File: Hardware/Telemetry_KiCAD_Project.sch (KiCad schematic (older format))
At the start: 3 parts, among them J1 TX SPI Debug, J2 RX SPI Debug, J3 50Ω SMA Connector

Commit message: Placed RF traces w/rounded corners
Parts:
- J1, J2: footprint Connector_PinHeader_2.54mm:PinHeader_2x03_P2.54mm_Vertical -> Connector_PinHeader_2.54mm:PinHeader_2x04_P2.54mm_Vertical; symbol Connector_Generic:Conn_02x03_Odd_Even -> Connector_Generic:Conn_02x04_Odd_Even
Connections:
- net GND: now also J1.8 (Pin_8), J2.8 (Pin_8); no longer J1.6 (Pin_6), J2.6 (Pin_6)
- net RX_RST: now also J2.1 (Pin_1)
- net RX_SCL: now also J2.5 (Pin_5); no longer J2.4 (Pin_4)
- net RX_SDI: now also J2.3 (Pin_3); no longer J2.2 (Pin_2)
- net RX_SDO: now also J2.4 (Pin_4); no longer J2.5 (Pin_5)
- net TX_RST: now also J1.1 (Pin_1)
- net TX_SCL: now also J1.5 (Pin_5); no longer J1.4 (Pin_4)
- net TX_SDI: now also J1.3 (Pin_3); no longer J1.2 (Pin_2)
- net TX_SDO: now also J1.4 (Pin_4); no longer J1.5 (Pin_5)
- net ~RX_IRQ: now also J2.6 (Pin_6); no longer J2.3 (Pin_3)
- net ~RX_SEL: now also J2.2 (Pin_2); no longer J2.1 (Pin_1)
- net ~TX_IRQ: now also J1.6 (Pin_6); no longer J1.3 (Pin_3)
- net ~TX_SEL: now also J1.2 (Pin_2); no longer J1.1 (Pin_1)
- no-connect marks 1 -> 3
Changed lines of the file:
@@
 	7050 3900 8350 3900
 $Comp
-L Connector_Generic:Conn_02x03_Odd_Even J1
-U 1 1 61BF0412
-P 4250 950
-F 0 "J1" H 4300 1267 50  0000 C CNN
-F 1 "TX SPI Debug" H 4300 1176 50  0000 C CNN
-F 2 "Connector_PinHeader_2.54mm:PinHeader_2x03_P2.54mm_Vertical" H 4250 950 50  0001 C CNN
-F 3 "~" H 4250 950 50  0001 C CNN
-	1    4250 950
-	1    0    0    -1
-$EndComp
-$Comp
-L Connector_Generic:Conn_02x03_Odd_Even J2
+L Connector_Generic:Conn_02x04_Odd_Even J2
 U 1 1 61BF15AF
 P 5750 950
 F 0 "J2" H 5800 1267 50  0000 C CNN
 F 1 "RX SPI Debug" H 5800 1176 50  0000 C CNN
-F 2 "Connector_PinHeader_2.54mm:PinHeader_2x03_P2.54mm_Vertical" H 5750 950 50  0001 C CNN
+F 2 "Connector_PinHeader_2.54mm:PinHeader_2x04_P2.54mm_Vertical" H 5750 950 50  0001 C CNN
 F 3 "~" H 5750 950 50  0001 C CNN
 	1    5750 950
 	1    0    0    -1
 $EndComp
-Text Label 4050 850  2    50   ~ 0
+Text Label 4550 850  0    50   ~ 0
 ~TX_SEL
+Text Label 4550 1050 0    50   ~ 0
+~TX_IRQ
+Text Label 4550 950  0    50   ~ 0
+TX_SDO
 Text Label 4050 950  2    50   ~ 0
-~TX_IRQ
+TX_SDI
 Text Label 4050 1050 2    50   ~ 0
-TX_SDO
-Text Label 4550 850  0    50   ~ 0
-TX_SDI
-Text Label 4550 950  0    50   ~ 0
 TX_SCL
-$Comp
-L power:GND #PWR01
-U 1 1 61BF6E76
-P 4550 1050
-F 0 "#PWR01" H 4550 800 50  0001 C CNN
-F 1 "GND" H 4555 877 50  0000 C CNN
-F 2 "" H 4550 1050 50  0001 C CNN
-F 3 "" H 4550 1050 50  0001 C CNN
-	1    4550 1050
-	1    0    0    -1
-$EndComp
-Text Label 5550 850  2    50   ~ 0
+Text Label 6050 850  0    50   ~ 0
 ~RX_SEL
+Text Label 6050 1050 0    50   ~ 0
+~RX_IRQ
+Text Label 6050 950  0    50   ~ 0
+RX_SDO
 Text Label 5550 950  2    50   ~ 0
-~RX_IRQ
+RX_SDI
 Text Label 5550 1050 2    50   ~ 0
-RX_SDO
-Text Label 6050 850  0    50   ~ 0
-RX_SDI
-Text Label 6050 950  0    50   ~ 0
 RX_SCL
 $Comp
 L power:GND #PWR02
 U 1 1 61BF7DA6
-P 6050 1050
-F 0 "#PWR02" H 6050 800 50  0001 C CNN
-F 1 "GND" H 6055 877 50  0000 C CNN
-F 2 "" H 6050 1050 50  0001 C CNN
-F 3 "" H 6050 1050 50  0001 C CNN
-	1    6050 1050
+P 6050 1150
+F 0 "#PWR02" H 6050 900 50  0001 C CNN
+F 1 "GND" H 6055 977 50  0000 C CNN
+F 2 "" H 6050 1150 50  0001 C CNN
+F 3 "" H 6050 1150 50  0001 C CNN
+	1    6050 1150
 	1    0    0    -1
 $EndComp
@@
 Entry Wire Line
 	6350 850  6450 950
-Entry Wire Line
-	6350 950  6450 1050
 Wire Bus Line
 	4800 2250 5550 2250
@@
 Text Label 6250 4400 2    50   ~ 0
 RX_RST
+$Comp
+L Connector_Generic:Conn_02x04_Odd_Even J1
+U 1 1 61BF0412
+P 4250 950
+F 0 "J1" H 4300 1267 50  0000 C CNN
+F 1 "TX SPI Debug" H 4300 1176 50  0000 C CNN
+F 2 "Connector_PinHeader_2.54mm:PinHeader_2x04_P2.54mm_Vertical" H 4250 950 50  0001 C CNN
+F 3 "~" H 4250 950 50  0001 C CNN
+	1    4250 950
+	1    0    0    -1
+$EndComp
+$Comp
+L power:GND #PWR01
+U 1 1 61BF6E76
+P 4550 1150
+F 0 "#PWR01" H 4550 900 50  0001 C CNN
+F 1 "GND" H 4555 977 50  0000 C CNN
+F 2 "" H 4550 1150 50  0001 C CNN
+F 3 "" H 4550 1150 50  0001 C CNN
+	1    4550 1150
+	1    0    0    -1
+$EndComp
+Entry Wire Line
+	6350 1050 6450 1150
+Entry Wire Line
+	6350 950  6450 1050
+Wire Wire Line
+	6350 1050 6050 1050
+Entry Wire Line
+	4850 1050 4950 1150
+Wire Wire Line
+	4850 1050 4550 1050
+Text Label 5550 850  2    50   ~ 0
+RX_RST
+Text Label 4050 850  2    50   ~ 0
+TX_RST
+NoConn ~ 5550 1150
+NoConn ~ 4050 1150
+Wire Bus Line
+	5150 950  5150 1400
+Wire Bus Line
+	3650 950  3650 1400
 Wire Bus Line
 	6450 950  6450 1400
@@
 	4950 950  4950 1400
 Wire Bus Line
-	5150 950  5150 1400
-Wire Bus Line
-	3650 950  3650 1400
-Wire Bus Line
 	4550 3450 4550 4200

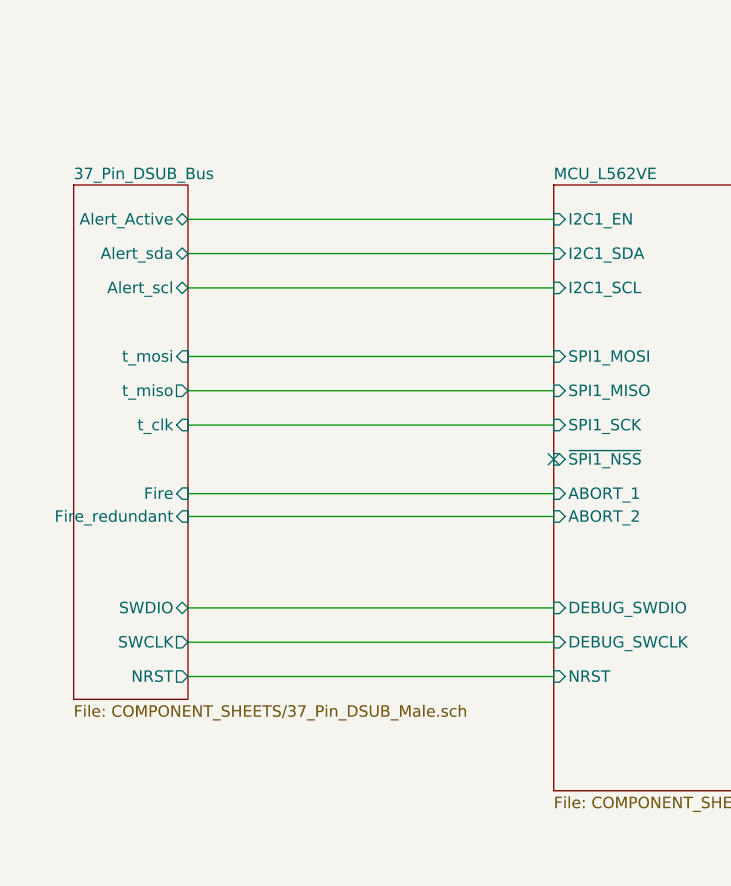
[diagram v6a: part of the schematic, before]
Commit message: Updated DSUB connector assignments
Welp, looks like everything got turned upside down, time to flip everything on the board, ugh
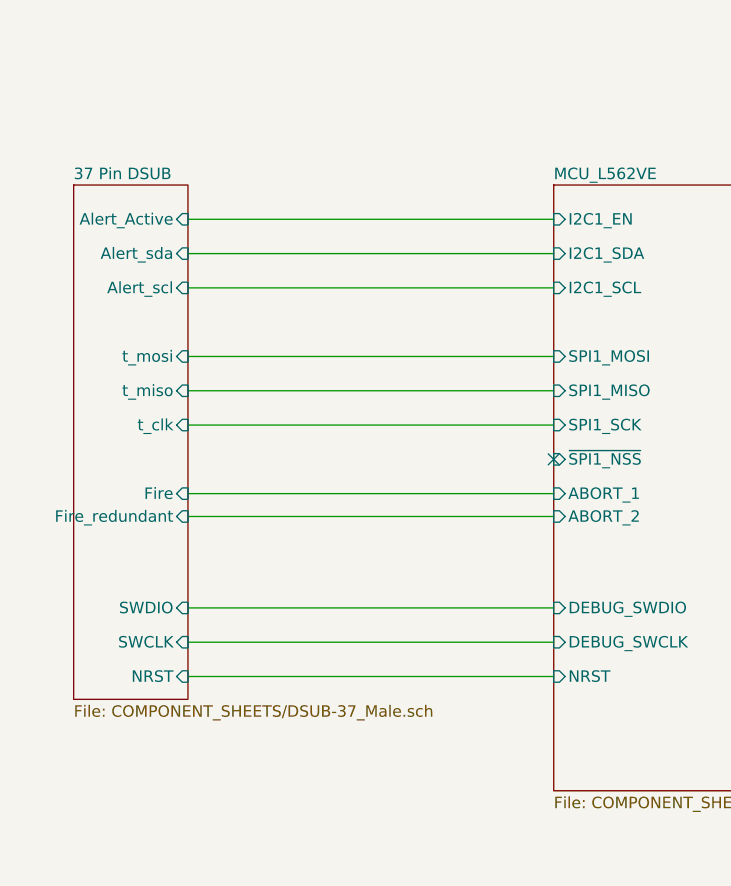
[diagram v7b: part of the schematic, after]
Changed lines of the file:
@@
 	4750 4600 4100 4600
-$Sheet
-S 750  2100 500  2250
-U 619DC150
-F0 "37_Pin_DSUB_Bus" 50
-F1 "COMPONENT_SHEETS/37_Pin_DSUB_Male.sch" 50
-F2 "t_mosi" I R 1250 2850 50
-F3 "t_clk" I R 1250 3150 50
-F4 "Fire" I R 1250 3450 50
-F5 "Fire_redundant" I R 1250 3550 50
-F6 "Alert_Active" B R 1250 2250 50
-F7 "Alert_scl" B R 1250 2550 50
-F8 "Alert_sda" B R 1250 2400 50
-F9 "t_miso" O R 1250 3000 50
-F10 "SWDIO" B R 1250 3950 50
-F11 "SWCLK" O R 1250 4100 50
-F12 "NRST" O R 1250 4250 50
-$EndSheet
 $Sheet
 S 2850 2100 1250 2650
@@
 Wire Bus Line
 	4550 2250 4550 3050
+$Sheet
+S 750  2100 500  2250
+U 61C225AD
+F0 "37 Pin DSUB" 50
+F1 "COMPONENT_SHEETS/DSUB-37_Male.sch" 50
+F2 "t_mosi" I R 1250 2850 50
+F3 "t_miso" I R 1250 3000 50
+F4 "t_clk" I R 1250 3150 50
+F5 "Alert_scl" I R 1250 2550 50
+F6 "Alert_sda" I R 1250 2400 50
+F7 "Alert_Active" I R 1250 2250 50
+F8 "SWDIO" I R 1250 3950 50
+F9 "SWCLK" I R 1250 4100 50
+F10 "NRST" I R 1250 4250 50
+F11 "Fire" I R 1250 3450 50
+F12 "Fire_redundant" I R 1250 3550 50
+$EndSheet
 $EndSCHEMATC

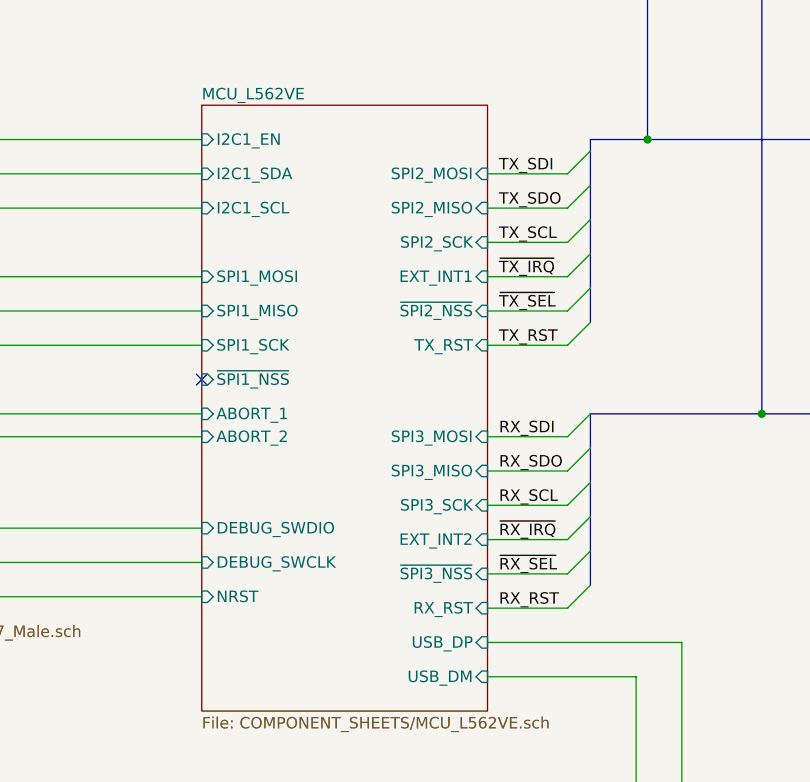
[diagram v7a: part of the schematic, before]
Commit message: Swapped SPI2 and SPI3 for TX/RX chips
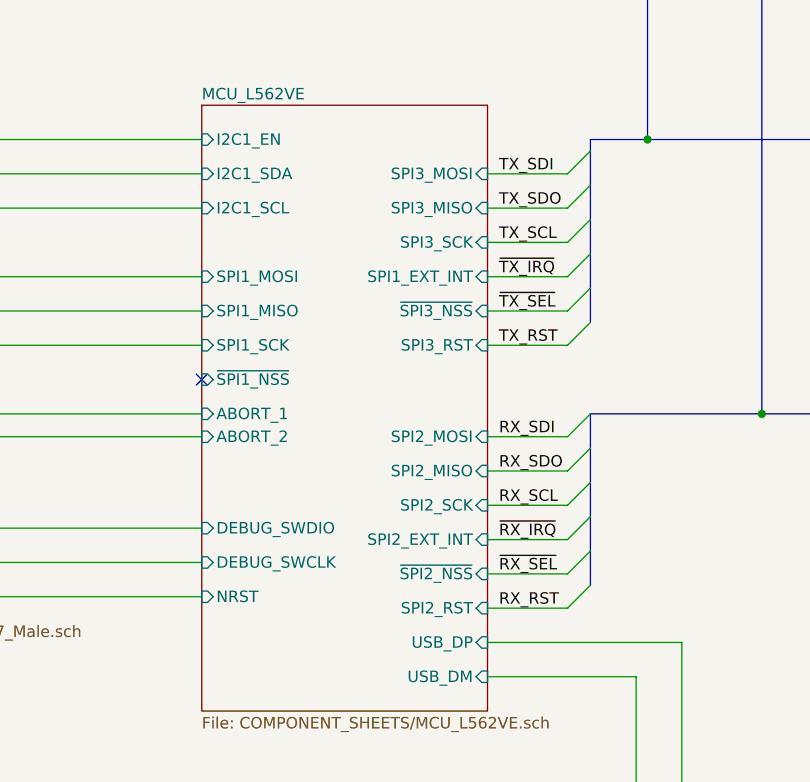
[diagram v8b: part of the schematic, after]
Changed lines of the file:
@@
 F4 "I2C1_EN" I L 2850 2250 50
 F5 "DEBUG_SWCLK" I L 2850 4100 50
-F6 "~SPI2_NSS" I R 4100 3000 50
-F7 "SPI3_MOSI" I R 4100 3550 50
-F8 "SPI3_MISO" I R 4100 3700 50
-F9 "SPI3_SCK" I R 4100 3850 50
+F6 "~SPI2_NSS" I R 4100 4150 50
+F7 "SPI3_MOSI" I R 4100 2400 50
+F8 "SPI3_MISO" I R 4100 2550 50
+F9 "SPI3_SCK" I R 4100 2700 50
 F10 "DEBUG_SWDIO" I L 2850 3950 50
 F11 "USB_DP" I R 4100 4450 50
 F12 "USB_DM" I R 4100 4600 50
-F13 "SPI2_SCK" I R 4100 2700 50
-F14 "SPI2_MISO" I R 4100 2550 50
-F15 "SPI2_MOSI" I R 4100 2400 50
-F16 "~SPI3_NSS" I R 4100 4150 50
+F13 "SPI2_SCK" I R 4100 3850 50
+F14 "SPI2_MISO" I R 4100 3700 50
+F15 "SPI2_MOSI" I R 4100 3550 50
+F16 "~SPI3_NSS" I R 4100 3000 50
 F17 "SPI1_SCK" I L 2850 3150 50
 F18 "SPI1_MISO" I L 2850 3000 50
 F19 "SPI1_MOSI" I L 2850 2850 50
 F20 "~SPI1_NSS" I L 2850 3300 50
-F21 "EXT_INT1" I R 4100 2850 50
-F22 "NRST" I L 2850 4250 50
-F23 "ABORT_1" I L 2850 3450 50
-F24 "ABORT_2" I L 2850 3550 50
-F25 "EXT_INT2" I R 4100 4000 50
-F26 "RX_RST" I R 4100 4300 50
-F27 "TX_RST" I R 4100 3150 50
+F21 "NRST" I L 2850 4250 50
+F22 "ABORT_1" I L 2850 3450 50
+F23 "ABORT_2" I L 2850 3550 50
+F24 "SPI2_RST" I R 4100 4300 50
+F25 "SPI3_RST" I R 4100 3150 50
+F26 "SPI2_EXT_INT" I R 4100 4000 50
+F27 "SPI1_EXT_INT" I R 4100 2850 50
 $EndSheet
 Wire Wire Line
